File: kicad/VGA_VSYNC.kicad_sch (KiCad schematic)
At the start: 11 parts, among them U28 74LS163, U29 74LS163, U3 74LS00, U30 74LS163, U31 74LS04, U32 74LS04, U33 74LS30, U34 74LS30, U35 74LS30

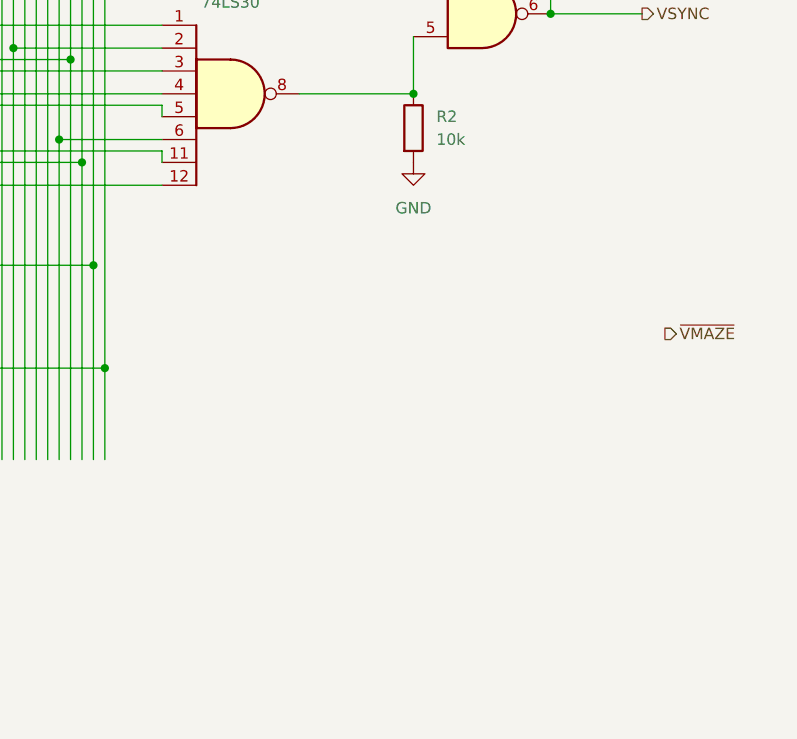
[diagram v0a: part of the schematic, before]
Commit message: Add AT28C64 symbol. Tidy up HSYNC schematic. Add EEPROM - Z80 connection and VGA - Z80 connection
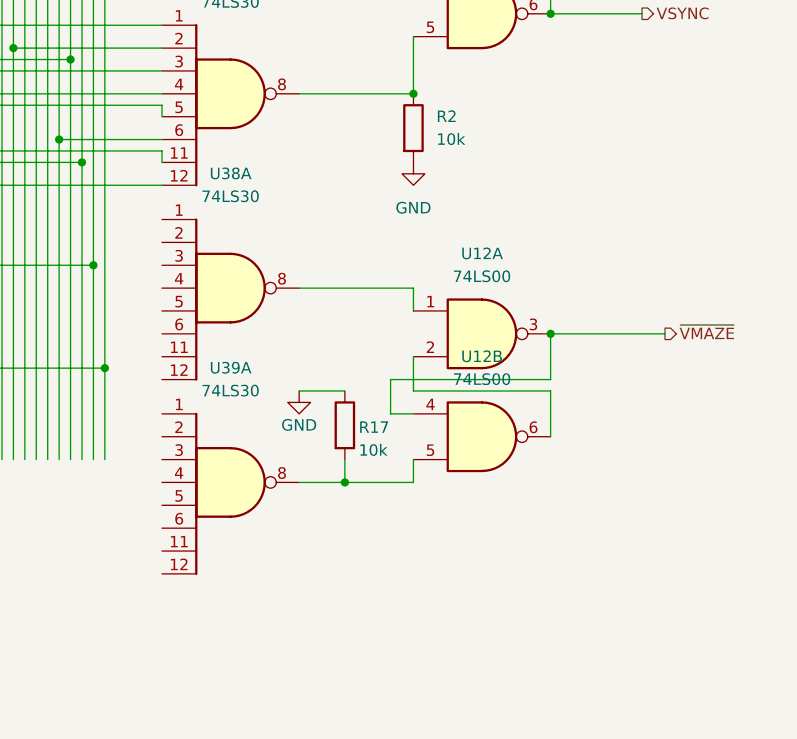
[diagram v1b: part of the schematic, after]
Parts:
- added R17: 10k, symbol Device:R
- added U12: 74LS00, symbol 74xx:74LS00
- added U38, U39: 74LS30, symbol 74xx:74LS30
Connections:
- net GND: now also R17.1
- net ~{VMAZE}: now also U12.3, U12.4
- new net: U12.1, U38.8
- new net: R17.2, U12.5, U39.8
- new net: U12.2, U12.6
